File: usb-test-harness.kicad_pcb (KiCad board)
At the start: 2 copper layers, 73 x 85 mm, 9 parts, among them J1 USB_A (female up), J2 USB_B_Micro (up), J3 USB_A (male down), J4 USB_A (female down), J5 USB_A_DUAL, J6 USB_A_DUAL, J7 USB_A_DUAL, U1 USB2514B_Bi, U2 USB2514B_Bi

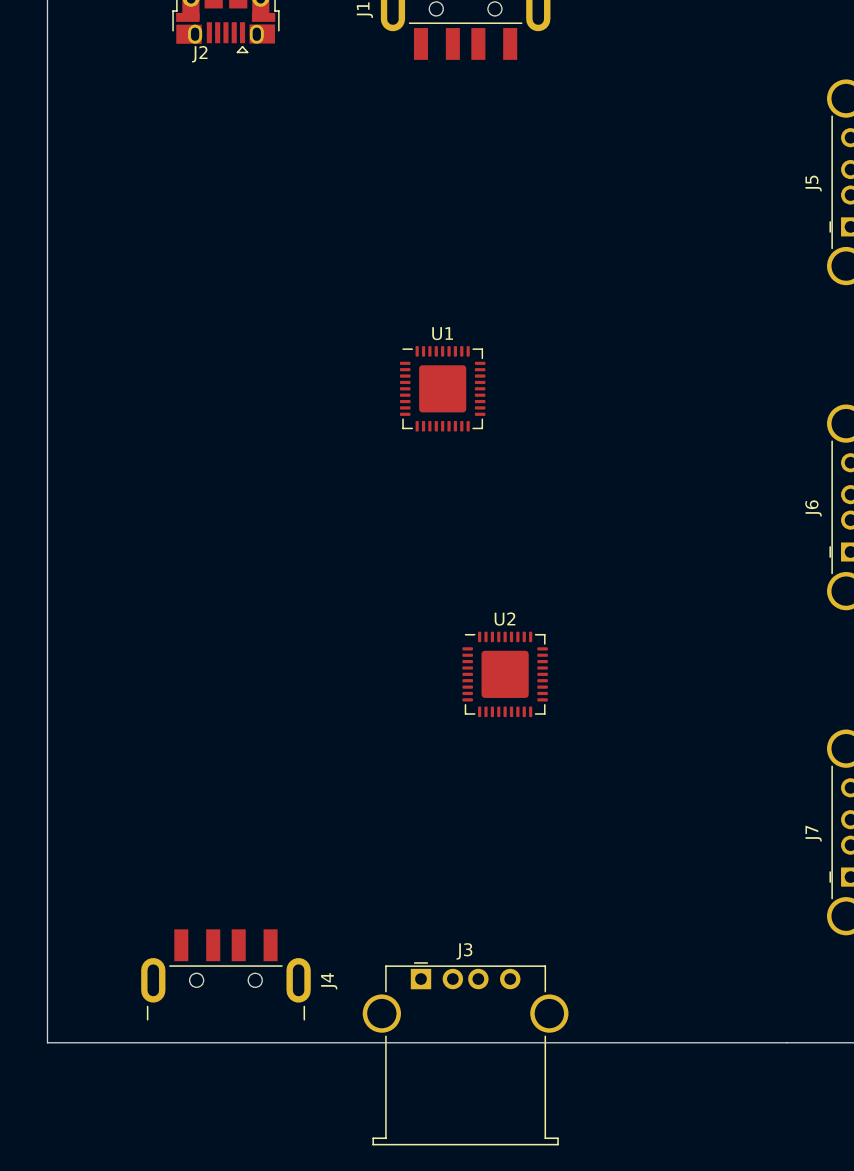
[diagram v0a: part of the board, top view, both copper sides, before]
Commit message: hw: usb-test-harness: more hacking on a hub
this is insane.
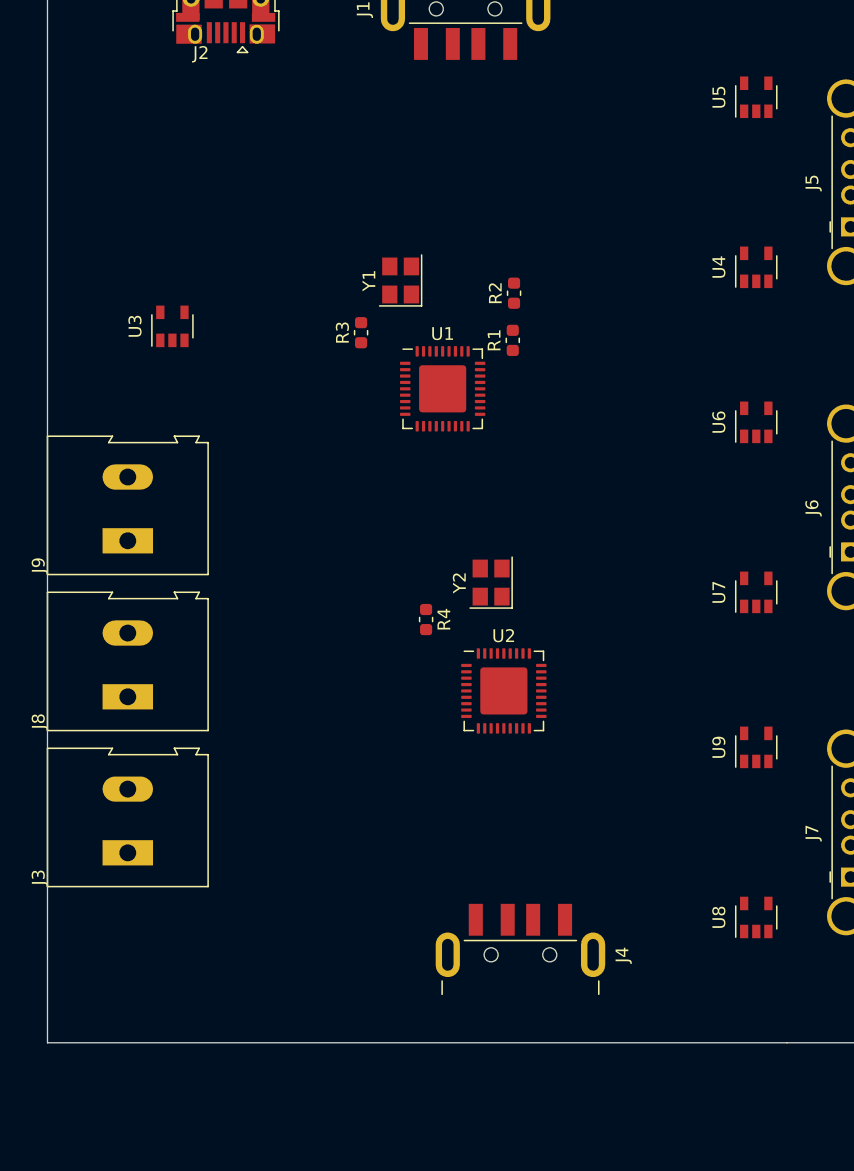
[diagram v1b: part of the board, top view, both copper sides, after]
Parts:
- added J8: 5V_RAW, TerminalBlock:TerminalBlock_Altech_AK300-2_P5.00mm, F.Cu at (110.3, 117.9)
- added J9: GND, TerminalBlock:TerminalBlock_Altech_AK300-2_P5.00mm, F.Cu at (110.3, 105.6)
- added R1: 100k, Resistor_SMD:R_0603_1608Metric, F.Cu at (140.5, 89.9)
- added R2: 100k, Resistor_SMD:R_0603_1608Metric, F.Cu at (140.6, 86.2)
- added R3: 12k, Resistor_SMD:R_0603_1608Metric, F.Cu at (128.6, 89.3)
- added R4: 12k, Resistor_SMD:R_0603_1608Metric, F.Cu at (133.7, 111.8)
- added U3: MIC5504-3.3YM5, Package_TO_SOT_SMD:SOT-23-5, F.Cu at (113.8, 88.8)
- added U4: APL3511C, Package_TO_SOT_SMD:SOT-23-5, F.Cu at (159.6, 84.2)
- added U5: APL3511C, Package_TO_SOT_SMD:SOT-23-5, F.Cu at (159.6, 70.8)
- added U6: APL3511C, Package_TO_SOT_SMD:SOT-23-5, F.Cu at (159.6, 96.3)
- added U7: APL3511C, Package_TO_SOT_SMD:SOT-23-5, F.Cu at (159.6, 109.7)
- added U8: APL3511C, Package_TO_SOT_SMD:SOT-23-5, F.Cu at (159.6, 135.2)
- added U9: APL3511C, Package_TO_SOT_SMD:SOT-23-5, F.Cu at (159.6, 121.8)
- added Y1: Crystal_GND23_Small, Crystal:Crystal_SMD_3225-4Pin_3.2x2.5mm, F.Cu at (131.7, 85.2)
- added Y2: Crystal_GND23_Small, Crystal:Crystal_SMD_3225-4Pin_3.2x2.5mm, F.Cu at (138.8, 108.9)
- J1: value USB_A (female up) -> USB_A (male up)
- J3: value USB_A (male down) -> Vext; footprint Connector_USB:USB_A_Stewart_SS-52100-001_Horizontal -> TerminalBlock:TerminalBlock_Altech_AK300-2_P5.00mm
- moved J3 25.0 mm to (110.3, 130.1), turned to 90 degrees
- moved J4 23.2 mm to (141.1, 145.0)
- moved U2 1.30 mm to (139.8, 117.4)
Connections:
- J1 pad 1: (no net) -> Net-(J1-Pad1)
- J2 pad 1: (no net) -> Net-(J1-Pad1)
- J3 pad 2: Net-(J4-Pad2) -> (no net)
- J5 pad 1: (no net) -> Net-(J5-Pad1)
- J5 pad 4: (no net) -> GND
- J5 pad 5: (no net) -> Net-(J5-Pad5)
- J5 pad 8: (no net) -> GND
- J6 pad 1: (no net) -> Net-(J6-Pad1)
- J6 pad 4: (no net) -> GND
- J6 pad 5: (no net) -> Net-(J6-Pad5)
- J6 pad 8: (no net) -> GND
- J7 pad 1: (no net) -> Net-(J7-Pad1)
- J7 pad 2: (no net) -> /U6+
- J7 pad 3: (no net) -> /U6+
- J7 pad 4: (no net) -> GND
- J7 pad 5: (no net) -> Net-(J7-Pad5)
- J7 pad 6: (no net) -> /U7-
- J7 pad 7: (no net) -> /U7+
- J7 pad 8: (no net) -> GND
- U1 pad 10: (no net) -> +3V3
- U1 pad 12: (no net) -> Net-(U1-Pad12)
- U1 pad 13: (no net) -> Net-(U1-Pad13)
- U1 pad 15: (no net) -> +3V3
- U1 pad 16: (no net) -> Net-(U1-Pad16)
- U1 pad 17: (no net) -> Net-(U1-Pad17)
- U1 pad 23: (no net) -> +3V3
- U1 pad 27: (no net) -> Net-(R1-Pad1)
- U1 pad 29: (no net) -> +3V3
- U1 pad 32: (no net) -> Net-(U1-Pad32)
- U1 pad 33: (no net) -> Net-(U1-Pad33)
- U1 pad 35: (no net) -> Net-(R3-Pad1)
- U1 pad 36: (no net) -> +3V3
- U1 pad 37: (no net) -> GND
- U1 pad 5: (no net) -> +3V3
- U1 pad 6: (no net) -> Net-(U1-Pad6)
- U1 pad 7: (no net) -> Net-(U1-Pad7)
- U1 pad 8: Net-(U1-Pad8) -> Net-(J4-Pad2)
- U1 pad 9: Net-(U1-Pad9) -> Net-(J4-Pad3)
- U2 pad 10: (no net) -> +3V3
- U2 pad 12: (no net) -> Net-(U2-Pad12)
- U2 pad 13: (no net) -> Net-(U2-Pad13)
- U2 pad 15: (no net) -> +3V3
- U2 pad 16: (no net) -> Net-(U2-Pad16)
- U2 pad 17: (no net) -> Net-(U2-Pad17)
- U2 pad 18: (no net) -> Net-(U2-Pad18)
- U2 pad 19: (no net) -> Net-(U2-Pad19)
- U2 pad 20: (no net) -> Net-(U2-Pad20)
- U2 pad 21: (no net) -> Net-(U2-Pad21)
- U2 pad 23: (no net) -> +3V3
- U2 pad 29: (no net) -> +3V3
- U2 pad 30: Net-(U1-Pad8) -> Net-(U1-Pad6)
- U2 pad 31: Net-(U1-Pad9) -> Net-(U1-Pad7)
- U2 pad 32: (no net) -> Net-(U2-Pad32)
- U2 pad 33: (no net) -> Net-(U2-Pad33)
- U2 pad 35: (no net) -> Net-(R4-Pad1)
- U2 pad 36: (no net) -> +3V3
- U2 pad 37: (no net) -> GND
- U2 pad 5: (no net) -> +3V3
- U2 pad 6: (no net) -> /U6+
- U2 pad 7: (no net) -> /U6+
- U2 pad 8: Net-(J4-Pad2) -> /U7-
- U2 pad 9: Net-(J4-Pad3) -> /U7+

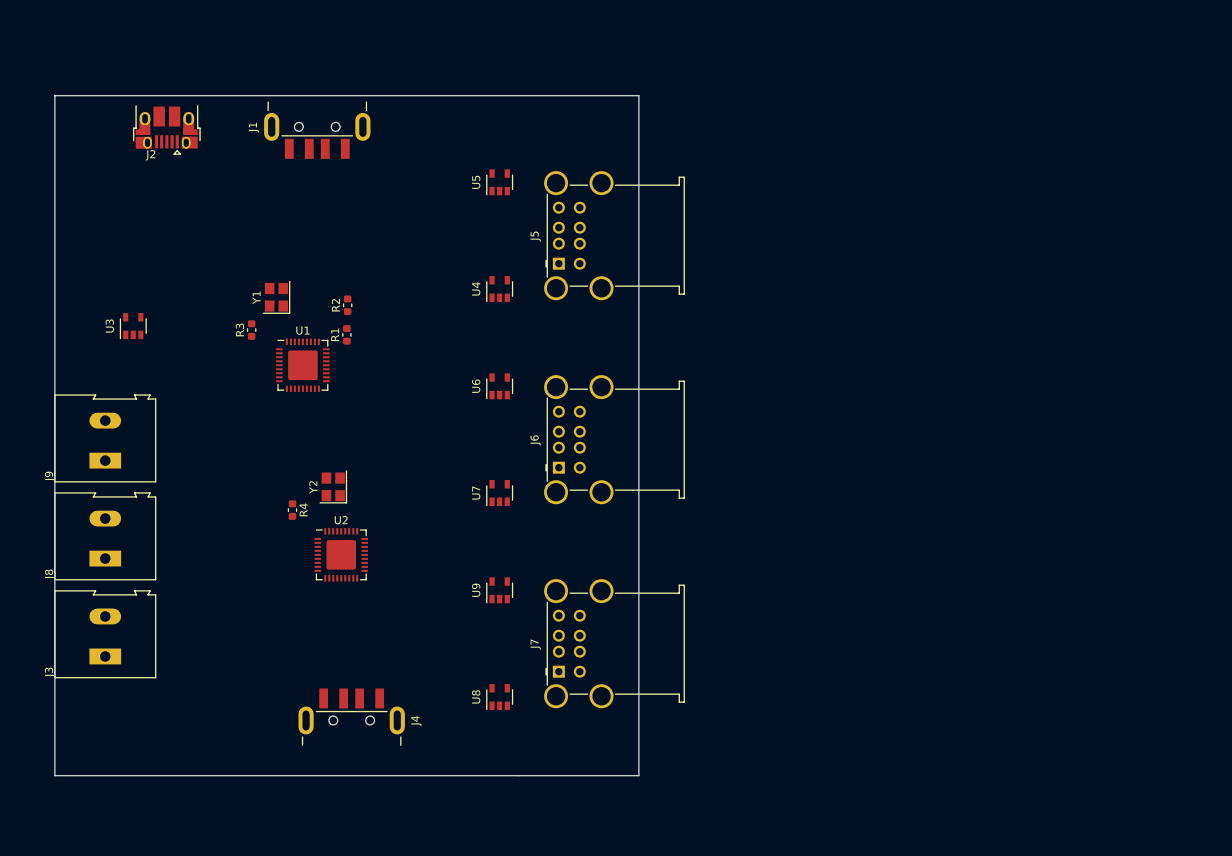
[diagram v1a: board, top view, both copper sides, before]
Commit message: usb-test-harness: updated usb footprints, working on it again
Just trying to finalise the connectors before getting down to brass
tacks
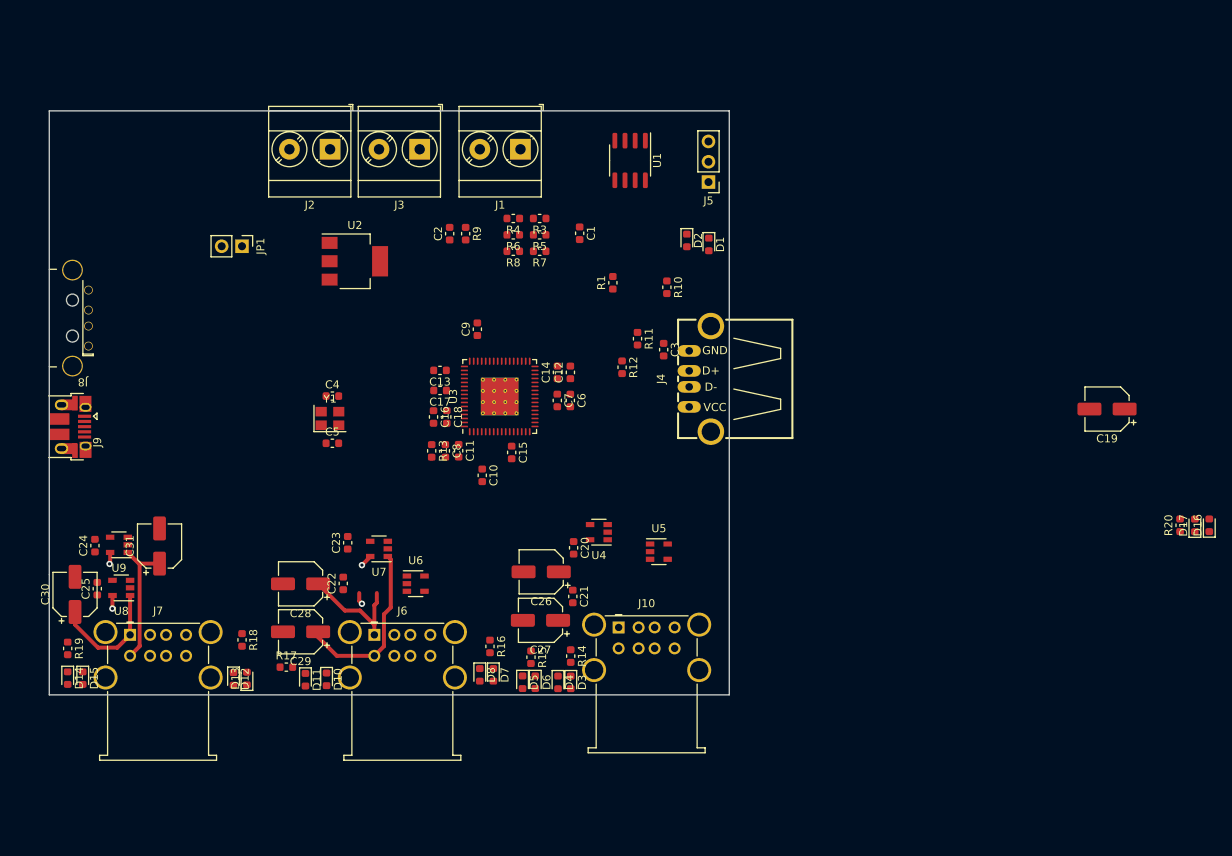
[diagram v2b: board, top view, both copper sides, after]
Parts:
- removed R2: 100k, Resistor_SMD:R_0603_1608Metric
- removed Y2: Crystal_GND23_Small, Crystal:Crystal_SMD_3225-4Pin_3.2x2.5mm
- added C1: .1uF, Capacitor_SMD:C_0603_1608Metric, F.Cu at (169.6, 77.2)
- added C10: .1uF, Capacitor_SMD:C_0603_1608Metric, F.Cu at (157.4, 107.5)
- added C11: .1uF, Capacitor_SMD:C_0603_1608Metric, F.Cu at (154.5, 104.4)
- added C12: 1uF, Capacitor_SMD:C_0603_1608Metric, F.Cu at (168.4, 94.6)
- added C13: .1uF, Capacitor_SMD:C_0603_1608Metric, F.Cu at (152.1, 94.3)
- added C14: .1uF, Capacitor_SMD:C_0603_1608Metric, F.Cu at (166.8, 94.6)
- added C15: .1uF, Capacitor_SMD:C_0603_1608Metric, F.Cu at (161.1, 104.6)
- added C16: 1uF, Capacitor_SMD:C_0603_1608Metric, F.Cu at (151.3, 100.2)
- added C17: .1uF, Capacitor_SMD:C_0603_1608Metric, F.Cu at (152.2, 96.8)
- added C18: .1uF, Capacitor_SMD:C_0603_1608Metric, F.Cu at (153.0, 100.2)
- added C19: 100uF, Capacitor_SMD:CP_Elec_5x5.4, F.Cu at (235.5, 99.2)
- added C2: .1uF, Capacitor_SMD:C_0603_1608Metric, F.Cu at (153.3, 77.2)
- added C20: 1uF, Capacitor_SMD:C_0603_1608Metric, F.Cu at (168.8, 116.5)
- added C21: 1uF, Capacitor_SMD:C_0603_1608Metric, F.Cu at (168.7, 122.6)
- added C22: 1uF, Capacitor_SMD:C_0603_1608Metric, F.Cu at (140.0, 121.0)
- added C23: 1uF, Capacitor_SMD:C_0603_1608Metric, F.Cu at (140.6, 115.9)
- added C24: 1uF, Capacitor_SMD:C_0603_1608Metric, F.Cu at (109.0, 116.2)
- added C25: 1uF, Capacitor_SMD:C_0603_1608Metric, F.Cu at (109.3, 121.6)
- added C26: 100uF, Capacitor_SMD:CP_Elec_5x5.4, F.Cu at (164.8, 119.5)
- added C27: 100uF, Capacitor_SMD:CP_Elec_5x5.4, F.Cu at (164.7, 125.6)
- added C28: 100uF, Capacitor_SMD:CP_Elec_5x5.4, F.Cu at (134.7, 121.0)
- added C29: 100uF, Capacitor_SMD:CP_Elec_5x5.4, F.Cu at (134.7, 127.0)
- added C3: 2.2uF, Capacitor_SMD:C_0603_1608Metric, F.Cu at (180.1, 91.8)
- added C30: 100uF, Capacitor_SMD:CP_Elec_5x5.4, F.Cu at (106.5, 122.3)
- added C31: 100uF, Capacitor_SMD:CP_Elec_5x5.4, F.Cu at (117.1, 116.3)
- added C4: 33pF, Capacitor_SMD:C_0603_1608Metric, F.Cu at (138.7, 97.5)
- added C5: 33pF, Capacitor_SMD:C_0603_1608Metric, F.Cu at (138.7, 103.5)
- added C6: 1uF, Capacitor_SMD:C_0603_1608Metric, F.Cu at (168.4, 98.1)
- added C7: .1uF, Capacitor_SMD:C_0603_1608Metric, F.Cu at (166.8, 98.1)
- added C8: 1uF, Capacitor_SMD:C_0603_1608Metric, F.Cu at (152.8, 104.4)
- added C9: .1uF, Capacitor_SMD:C_0603_1608Metric, F.Cu at (156.8, 89.2)
- added D1: HS1B, LED_SMD:LED_0603_1608Metric, F.Cu at (185.8, 78.6)
- added D10: G4, LED_SMD:LED_0603_1608Metric, F.Cu at (138.0, 133.0)
- added D11: R4, LED_SMD:LED_0603_1608Metric, F.Cu at (135.3, 133.0)
- added D12: G5, LED_SMD:LED_0603_1608Metric, F.Cu at (126.3, 132.9)
- added D13: R5, LED_SMD:LED_0603_1608Metric, F.Cu at (128.0, 132.9)
- added D14: G6, LED_SMD:LED_0603_1608Metric, F.Cu at (105.6, 132.8)
- added D15: R6, LED_SMD:LED_0603_1608Metric, F.Cu at (107.5, 132.8)
- added D16: G7, LED_SMD:LED_0603_1608Metric, F.Cu at (248.3, 113.7)
- added D17: R7, LED_SMD:LED_0603_1608Metric, F.Cu at (246.5, 113.7)
- added D2: HS1A, LED_SMD:LED_0603_1608Metric, F.Cu at (183.0, 78.1)
- added D3: G1, LED_SMD:LED_0603_1608Metric, F.Cu at (168.5, 133.3)
- added D4: R1, LED_SMD:LED_0603_1608Metric, F.Cu at (166.9, 133.3)
- added D5: G2, LED_SMD:LED_0603_1608Metric, F.Cu at (162.5, 133.3)
- added D6: R2, LED_SMD:LED_0603_1608Metric, F.Cu at (164.1, 133.3)
- added D7: G3, LED_SMD:LED_0603_1608Metric, F.Cu at (158.8, 132.4)
- added D8: R3, LED_SMD:LED_0603_1608Metric, F.Cu at (157.1, 132.4)
- added J10: USB_A_DUAL, Connector_USB:USB_A_Wuerth_61400826021_Horizontal_Stacked, F.Cu at (174.5, 126.5)
- added JP1: Jumper_NO_Small, Connector_PinHeader_2.54mm:PinHeader_1x02_P2.54mm_Vertical, F.Cu at (127.4, 78.8)
- added R10: 330, Resistor_SMD:R_0603_1608Metric, F.Cu at (180.5, 84.0)
- added R11: 100k, Resistor_SMD:R_0603_1608Metric, F.Cu at (176.8, 90.4)
- added R12: 100k, Resistor_SMD:R_0603_1608Metric, F.Cu at (174.9, 94.0)
- added R13: 12k, Resistor_SMD:R_0603_1608Metric, F.Cu at (151.1, 104.4)
- added R14: 330, Resistor_SMD:R_0603_1608Metric, F.Cu at (168.5, 130.1)
- added R15: 330, Resistor_SMD:R_0603_1608Metric, F.Cu at (163.5, 130.2)
- added R16: 330, Resistor_SMD:R_0603_1608Metric, F.Cu at (158.4, 128.8)
- added R17: 330, Resistor_SMD:R_0603_1608Metric, F.Cu at (132.9, 131.4)
- added R18: 330, Resistor_SMD:R_0603_1608Metric, F.Cu at (127.4, 128.0)
- added R19: 330, Resistor_SMD:R_0603_1608Metric, F.Cu at (105.6, 129.1)
- added R20: 330, Resistor_SMD:R_0603_1608Metric, F.Cu at (244.7, 113.7)
- added R5: 10k, Resistor_SMD:R_0603_1608Metric, F.Cu at (164.6, 77.4)
- added R6: 10k, Resistor_SMD:R_0603_1608Metric, F.Cu at (161.3, 77.4)
- added R7: 10k, Resistor_SMD:R_0603_1608Metric, F.Cu at (164.6, 79.5)
- added R8: 10k, Resistor_SMD:R_0603_1608Metric, F.Cu at (161.3, 79.5)
- added R9: 100k, Resistor_SMD:R_0603_1608Metric, F.Cu at (155.3, 77.2)
- J1: value USB_A (male up) -> 5V_RAW; footprint Connector_USB:USB_A_Receptacle_GENERIC -> TerminalBlock_Phoenix:TerminalBlock_Phoenix_MKDS-3-2-5.08_1x02_P5.08mm_Horizontal
- J2: value USB_B_Micro (up) -> GND; footprint Connector_USB:USB_Micro-B_Amphenol_10103594-0001LF_Horizontal -> TerminalBlock_Phoenix:TerminalBlock_Phoenix_MKDS-3-2-5.08_1x02_P5.08mm_Horizontal
- J3: value Vext -> V_EXT; footprint TerminalBlock:TerminalBlock_Altech_AK300-2_P5.00mm -> TerminalBlock_Phoenix:TerminalBlock_Phoenix_MKDS-3-2-5.08_1x02_P5.08mm_Horizontal
- J4: footprint Connector_USB:USB_A_Receptacle_GENERIC -> OPL_Connector:USB4+2P-2.0-90D
- J5: value USB_A_DUAL -> Conn_01x03_Male; footprint Connector_USB:USB_A_Wuerth_61400826021_Horizontal_Stacked -> Connector_PinHeader_2.54mm:PinHeader_1x03_P2.54mm_Vertical
- J8: value 5V_RAW -> USB_A (male up); footprint TerminalBlock:TerminalBlock_Altech_AK300-2_P5.00mm -> Connector_USB:USB_A_Plug_SOFNG_USB-05
- J9: value GND -> USB_B_Micro (up); footprint TerminalBlock:TerminalBlock_Altech_AK300-2_P5.00mm -> Connector_USB:USB_Micro-B_Amphenol_10103594-0001LF_Horizontal
- R1: value 100k -> 10k
- R3, R4: value 12k -> 10k
- U1: value USB2514B_Bi -> FT24C02A; footprint Package_DFN_QFN:QFN-36-1EP_6x6mm_P0.5mm_EP3.7x3.7mm -> Package_SO:SOIC-8_3.9x4.9mm_P1.27mm
- U2: value USB2514B_Bi -> SE5120ST33; footprint Package_DFN_QFN:QFN-36-1EP_6x6mm_P0.5mm_EP3.7x3.7mm -> Package_TO_SOT_SMD:SOT-223-3_TabPin2
- U3: value MIC5504-3.3YM5 -> USB2517; footprint Package_TO_SOT_SMD:SOT-23-5 -> Package_DFN_QFN:QFN-64-1EP_9x9mm_P0.5mm_EP4.7x4.7mm_ThermalVias
- Y1: value Crystal_GND23_Small -> 24MHz
- moved J3 74.6 mm to (149.6, 66.7), turned to 180 degrees
- moved J4 66.9 mm to (186.0, 95.4), turned to 90 degrees
- moved J7 53.8 mm to (113.4, 127.4), turned to 0 degrees
- moved U5 50.3 mm to (179.5, 117.0), turned to 0 degrees
- moved U8 49.2 mm to (112.3, 121.5), turned to 180 degrees
- moved U1 48.3 mm to (175.9, 68.1), turned to -90 degrees
- moved U9 47.9 mm to (112.0, 116.1), turned to 180 degrees
- moved U3 46.6 mm to (159.6, 97.6)
- moved R4 45.7 mm to (161.3, 75.3), turned to 180 degrees
- moved R3 38.6 mm to (164.6, 75.3), turned to 180 degrees
- moved U2 36.7 mm to (141.5, 80.7)
- moved R1 33.9 mm to (173.8, 83.4)
- moved U4 32.8 mm to (172.0, 114.6), turned to 180 degrees
- moved J6 31.1 mm to (143.9, 127.4), turned to 0 degrees
- moved J8 30.3 mm to (106.2, 87.8), turned to 180 degrees
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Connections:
- net Net-(J6-Pad1) renamed /downstream-port-power/VBUS3
- net Net-(J6-Pad5) renamed /downstream-port-power/VBUS4
- net Net-(J7-Pad1) renamed /downstream-port-power/VBUS5
- net Net-(J7-Pad5) renamed /downstream-port-power/VBUS6
- J1 pad 1: Net-(J1-Pad1) -> +5V
- J1 pad 2: Net-(J1-Pad2) -> +5V
- J2 pad 1: Net-(J1-Pad1) -> GND
- J2 pad 2: Net-(J1-Pad2) -> GND
- J3 pad 1: (no net) -> GND
- J4 pad 1: (no net) -> +5V
- J4 pad 2: Net-(J4-Pad2) -> /downstream-port-power/DS-
- J4 pad 3: Net-(J4-Pad3) -> /downstream-port-power/DS+
- J4 pad 4: (no net) -> GND
- J5 pad 1: Net-(J5-Pad1) -> /upstream-config-leds/EE_SDA
- J5 pad 2: (no net) -> /upstream-config-leds/CFG_SEL0
- J5 pad 3: (no net) -> GND
- J6 pad 2: (no net) -> /downstream-port-power/U3-
- J6 pad 3: (no net) -> /downstream-port-power/U3+
- J6 pad 6: (no net) -> /downstream-port-power/U4-
- J6 pad 7: (no net) -> /downstream-port-power/U4+
- J7 pad 2: /U6+ -> /downstream-port-power/U5-
- J7 pad 3: /U6+ -> /downstream-port-power/U5+
- J7 pad 6: /U7- -> /downstream-port-power/U6-
- J7 pad 7: /U7+ -> /downstream-port-power/U6+
- J8 pad 1: +5V -> /upstream-config-leds/VBUS_UP
- J8 pad 2: +5V -> /upstream-config-leds/UP-
- J9 pad 1: GND -> /upstream-config-leds/VBUS_UP
- J9 pad 2: GND -> /upstream-config-leds/UP-
- R1 pad 1: Net-(R1-Pad1) -> +3V3
- R1 pad 2: Net-(J1-Pad1) -> /upstream-config-leds/EE_SDA
- R3 pad 1: Net-(R3-Pad1) -> +3V3
- R3 pad 2: GND -> /upstream-config-leds/CFG_SEL2
- R4 pad 1: Net-(R4-Pad1) -> /upstream-config-leds/CFG_SEL2
- U1 pad 1: (no net) -> GND
- U1 pad 2: (no net) -> GND
- U1 pad 3: (no net) -> GND
- U1 pad 4: (no net) -> GND
- U1 pad 5: +3V3 -> /upstream-config-leds/EE_SDA
- U1 pad 6: Net-(U1-Pad6) -> /upstream-config-leds/CFG_SEL0
- U1 pad 7: Net-(U1-Pad7) -> GND
- U1 pad 8: Net-(J4-Pad2) -> +3V3
- U2 pad 1: (no net) -> GND
- U2 pad 2: (no net) -> +3V3
- U2 pad 3: (no net) -> +5V
- U3 pad 1: +5V -> /downstream-port-power/U3-
- U3 pad 2: GND -> /downstream-port-power/U3+
- U3 pad 3: +5V -> /downstream-port-power/U4-
- U3 pad 4: (no net) -> /downstream-port-power/U4+
- U4 pad 1: Net-(J5-Pad1) -> /downstream-port-power/VBUS1
- U4 pad 3: Net-(U1-Pad13) -> /downstream-port-power/OC1
- U4 pad 4: Net-(U1-Pad12) -> /downstream-port-power/EN1
- U5 pad 1: Net-(J5-Pad5) -> /downstream-port-power/VBUS2
- U5 pad 3: Net-(U1-Pad17) -> /downstream-port-power/OC2
- U5 pad 4: Net-(U1-Pad16) -> /downstream-port-power/EN2
- U6 pad 3: Net-(U2-Pad13) -> /downstream-port-power/OC3
- U6 pad 4: Net-(U2-Pad12) -> /downstream-port-power/EN3
- U7 pad 3: Net-(U2-Pad17) -> /downstream-port-power/OC4
- U7 pad 4: Net-(U2-Pad16) -> /downstream-port-power/EN4
- U8 pad 3: Net-(U2-Pad19) -> /downstream-port-power/OC5
- U8 pad 4: Net-(U2-Pad18) -> /downstream-port-power/EN5
- U9 pad 3: Net-(U2-Pad21) -> /downstream-port-power/OC6
- U9 pad 4: Net-(U2-Pad20) -> /downstream-port-power/EN6
- Y1 pad 1: Net-(U1-Pad33) -> /upstream-config-leds/XTAL2
- Y1 pad 2: (no net) -> GND
- Y1 pad 3: (no net) -> /upstream-config-leds/XTAL1
- Y1 pad 4: Net-(U1-Pad32) -> GND
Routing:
- net /downstream-port-power/VBUS4: track 0.00 -> 22.1 mm
- net /downstream-port-power/VBUS6: track 0.00 -> 16.6 mm
- net /downstream-port-power/VBUS5: track 0.00 -> 15.2 mm
- net /downstream-port-power/VBUS3: track 0.00 -> 14.5 mm
- net +5V: track 0.00 -> 6.09 mm, vias 0 -> 4
- added copper zone on In2.Cu, net +5V
- added copper zone on In1.Cu, net GND
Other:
- board size 73 x 85 mm -> 85 x 73 mm
- copper layers 2 -> 4
- net class usb-traces-4l added: clearance 1.27, trace_width 0.4064, via_dia 0.8, via_drill 0.4
